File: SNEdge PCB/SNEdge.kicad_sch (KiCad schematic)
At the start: 40 parts, among them J1 RGB_OUT, U1 THS7376

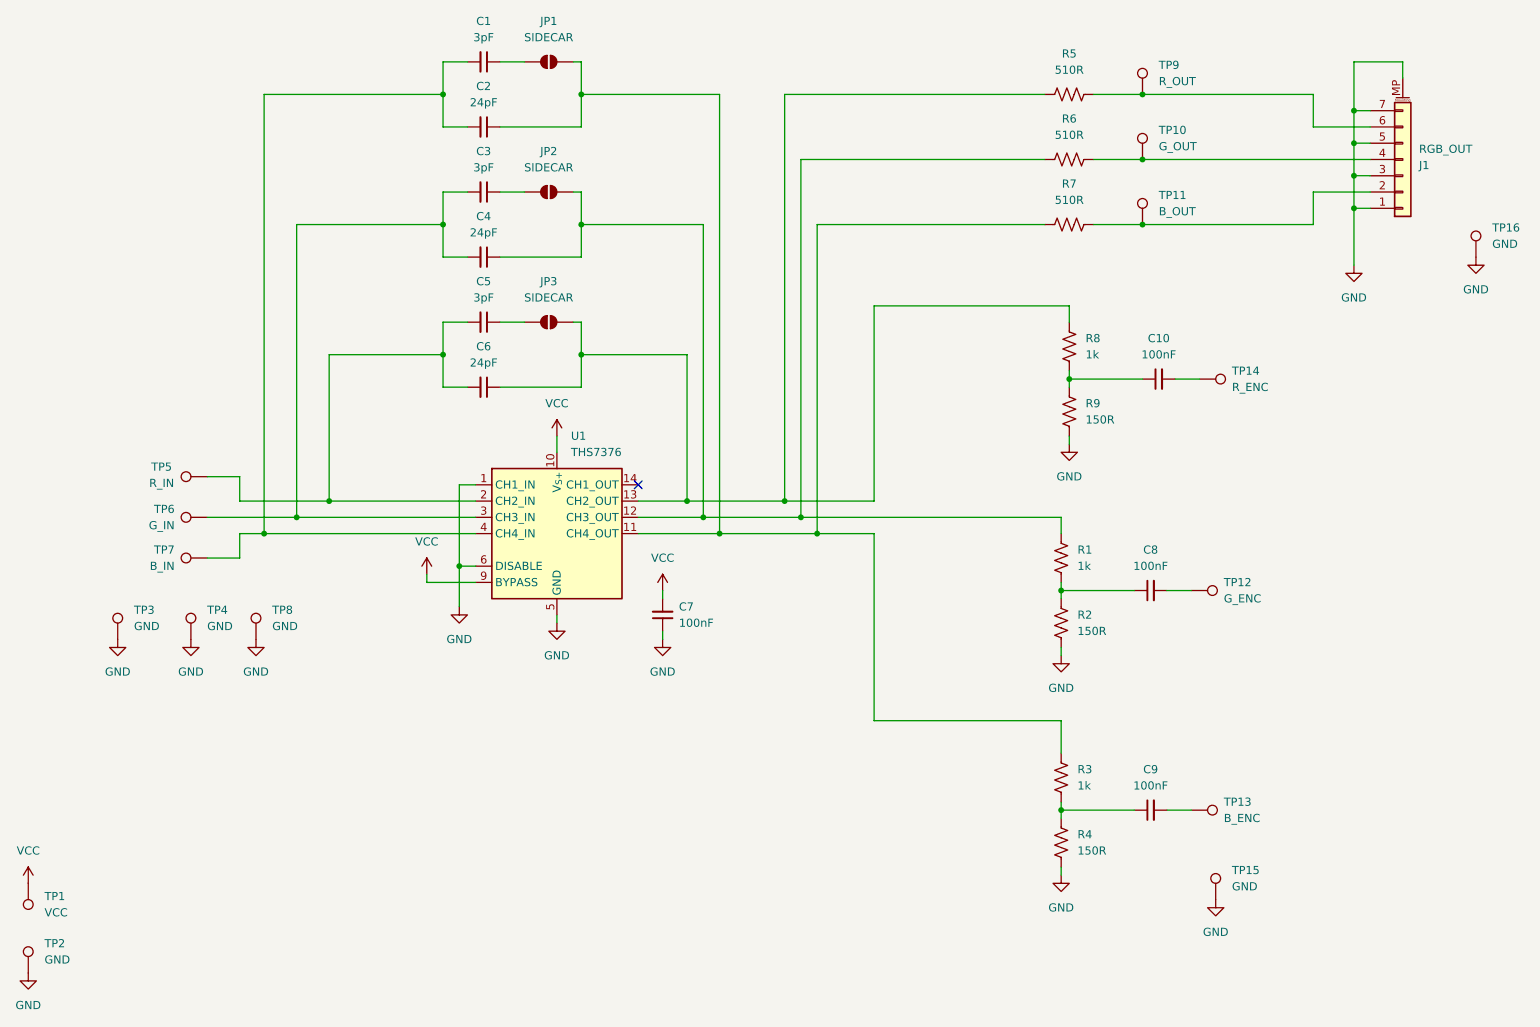
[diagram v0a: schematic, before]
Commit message: V2 based on RetroLoom's Rev2
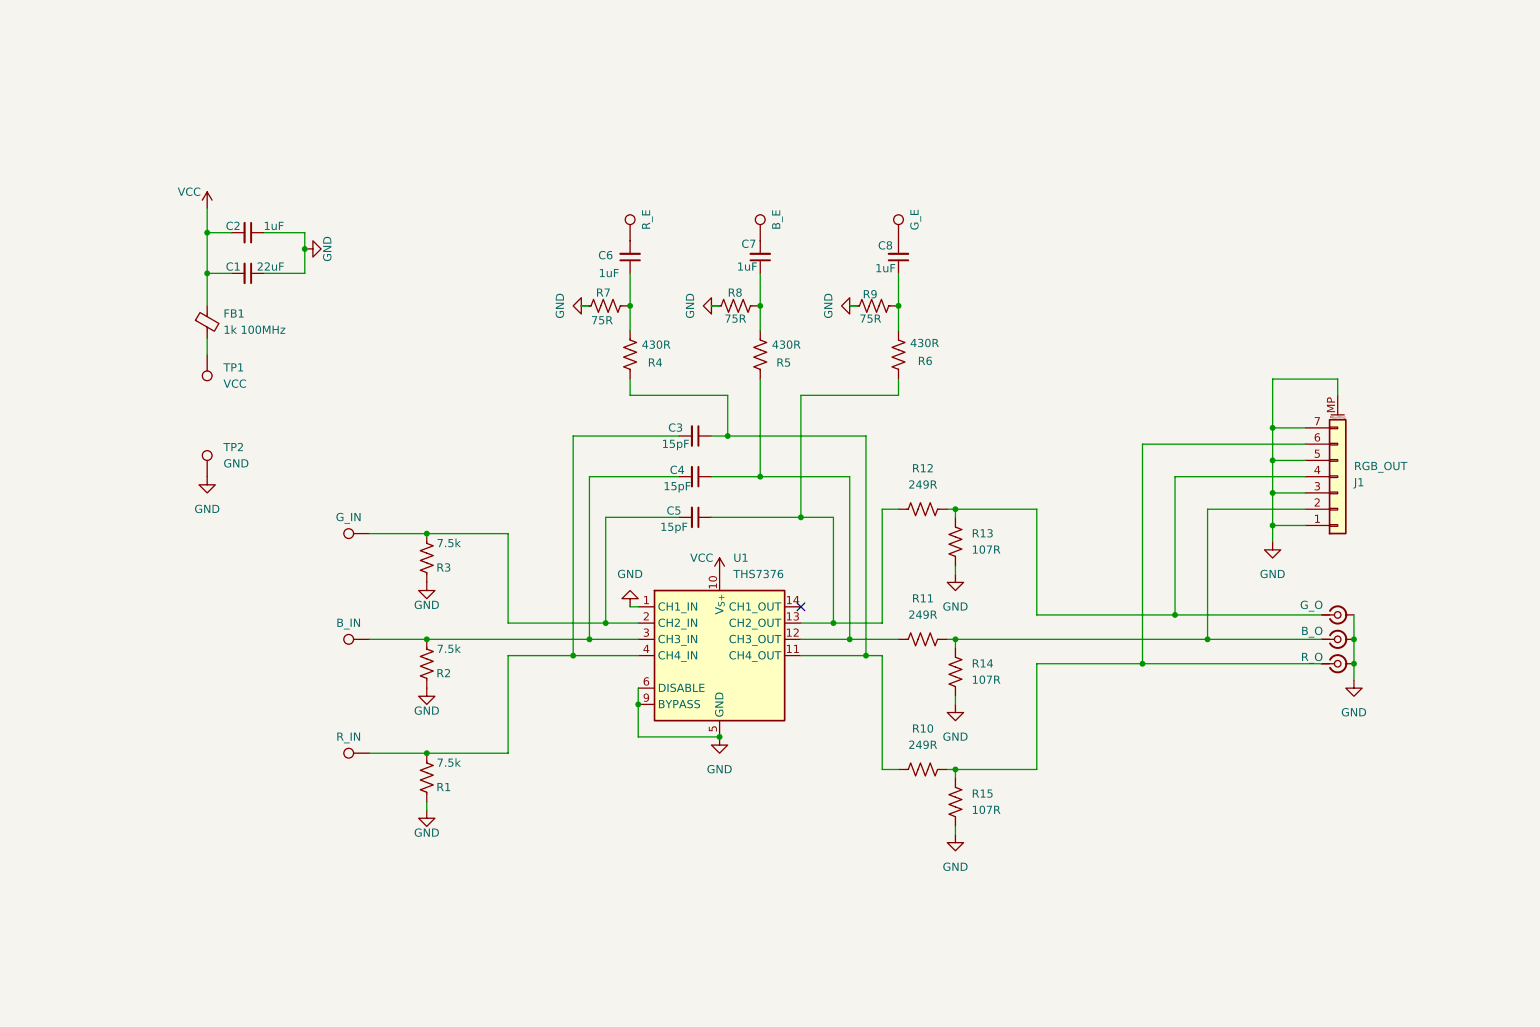
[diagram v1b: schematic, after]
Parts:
- removed C3, C5: 3pF, Capacitor_SMD:C_0805_2012Metric, symbol Device:C_Small
- removed C7: 100nF, Capacitor_SMD:C_0805_2012Metric, symbol Device:C_Small
- removed JP1, JP2, JP3: SIDECAR, Jumper:SolderJumper-2_P1.3mm_Open_RoundedPad1.0x1.5mm, symbol Jumper:SolderJumper_2_Open
- removed TP10: G_OUT, TestPoint:TestPoint_Pad_1.0x1.0mm, symbol Connector:TestPoint
- removed TP11: B_OUT, TestPoint:TestPoint_Pad_1.0x1.0mm, symbol Connector:TestPoint
- removed TP12: G_ENC, TestPoint:TestPoint_Pad_2.0x2.0mm, symbol Connector:TestPoint
- removed TP13: B_ENC, TestPoint:TestPoint_Pad_2.0x2.0mm, symbol Connector:TestPoint
- removed TP14: R_ENC, TestPoint:TestPoint_Pad_2.0x2.0mm, symbol Connector:TestPoint
- removed TP15: GND, TestPoint:TestPoint_Pad_2.0x2.0mm, symbol Connector:TestPoint
- removed TP16: GND, TestPoint:TestPoint_Pad_1.0x1.0mm, symbol Connector:TestPoint
- removed TP9: R_OUT, TestPoint:TestPoint_Pad_1.0x1.0mm, symbol Connector:TestPoint
- added C2: 1uF, Capacitor_SMD:C_0805_2012Metric_Pad1.18x1.45mm_HandSolder, symbol Device:C_Small
- added FB1: 1k 100MHz, Resistor_SMD:R_0805_2012Metric_Pad1.20x1.40mm_HandSolder, symbol Device:FerriteBead_Small
- added J10: R_O, Connector_Coaxial:U.FL_Hirose_U.FL-R-SMT-1_Vertical, symbol Connector:Conn_Coaxial_Small
- added J8: G_O, Connector_Coaxial:U.FL_Hirose_U.FL-R-SMT-1_Vertical, symbol Connector:Conn_Coaxial_Small
- added J9: B_O, Connector_Coaxial:U.FL_Hirose_U.FL-R-SMT-1_Vertical, symbol Connector:Conn_Coaxial_Small
- added R1, R2, R3: 7.5k, Resistor_SMD:R_0805_2012Metric_Pad1.20x1.40mm_HandSolder, symbol Device:R_US
- added R13, R14, R15: 107R, Resistor_SMD:R_0805_2012Metric_Pad1.20x1.40mm_HandSolder, symbol Device:R_US
- C1: value 3pF -> 22uF; footprint Capacitor_SMD:C_0805_2012Metric -> Capacitor_SMD:C_0805_2012Metric_Pad1.18x1.45mm_HandSolder; Digi_PN 311-1092-1-ND -> (none); MFG_PN CC0805CRNPO9BN3R0 -> (none)
- C3: renamed from C2; value 24pF -> 15pF; footprint Capacitor_SMD:C_0805_2012Metric -> Capacitor_SMD:C_0805_2012Metric_Pad1.18x1.45mm_HandSolder; Digi_PN 478-10387-1-ND -> (none); MFG_PN 08051A240FAT2A -> (none)
- C4: value 24pF -> 15pF; footprint Capacitor_SMD:C_0805_2012Metric -> Capacitor_SMD:C_0805_2012Metric_Pad1.18x1.45mm_HandSolder; Digi_PN 478-10387-1-ND -> (none); MFG_PN 08051A240FAT2A -> (none)
- C5: renamed from C6; value 24pF -> 15pF; footprint Capacitor_SMD:C_0805_2012Metric -> Capacitor_SMD:C_0805_2012Metric_Pad1.18x1.45mm_HandSolder; Digi_PN 478-10387-1-ND -> (none); MFG_PN 08051A240FAT2A -> (none)
- C6: renamed from C10; value 100nF -> 1uF; footprint Capacitor_SMD:C_0805_2012Metric -> Capacitor_SMD:C_0805_2012Metric_Pad1.18x1.45mm_HandSolder; Digi_PN 1276-2444-1-ND -> (none); MFG_PN CL21B104KBCNFNC -> (none)
- C7: renamed from C9; value 100nF -> 1uF; footprint Capacitor_SMD:C_0805_2012Metric -> Capacitor_SMD:C_0805_2012Metric_Pad1.18x1.45mm_HandSolder; Digi_PN 1276-2444-1-ND -> (none); MFG_PN CL21B104KBCNFNC -> (none)
- C8: value 100nF -> 1uF; footprint Capacitor_SMD:C_0805_2012Metric -> Capacitor_SMD:C_0805_2012Metric_Pad1.18x1.45mm_HandSolder; Digi_PN 1276-2444-1-ND -> (none); MFG_PN CL21B104KBCNFNC -> (none)
- R10: renamed from R7; value 510R -> 249R; footprint Resistor_SMD:R_0805_2012Metric -> Resistor_SMD:R_0805_2012Metric_Pad1.20x1.40mm_HandSolder; Digi_PN RMCF0805FT510RCT-ND -> (none); MFG_PN RMCF0805FT510R -> (none)
- R11: renamed from R6; value 510R -> 249R; footprint Resistor_SMD:R_0805_2012Metric -> Resistor_SMD:R_0805_2012Metric_Pad1.20x1.40mm_HandSolder; Digi_PN RMCF0805FT510RCT-ND -> (none); MFG_PN RMCF0805FT510R -> (none)
- R12: renamed from R5; value 510R -> 249R; footprint Resistor_SMD:R_0805_2012Metric -> Resistor_SMD:R_0805_2012Metric_Pad1.20x1.40mm_HandSolder; Digi_PN RMCF0805FT510RCT-ND -> (none); MFG_PN RMCF0805FT510R -> (none)
- R4: renamed from R8; value 1k -> 430R; footprint Resistor_SMD:R_0805_2012Metric -> Resistor_SMD:R_0805_2012Metric_Pad1.20x1.40mm_HandSolder; Digi_PN RMCF0805FT1K00CT-ND -> (none); MFG_PN RMCF0805FT1K00 -> (none)
- R5: renamed from R3; value 1k -> 430R; footprint Resistor_SMD:R_0805_2012Metric -> Resistor_SMD:R_0805_2012Metric_Pad1.20x1.40mm_HandSolder; Digi_PN RMCF0805FT1K00CT-ND -> (none); MFG_PN RMCF0805FT1K00 -> (none)
- R6: renamed from R1; value 1k -> 430R; footprint Resistor_SMD:R_0805_2012Metric -> Resistor_SMD:R_0805_2012Metric_Pad1.20x1.40mm_HandSolder; Digi_PN RMCF0805FT1K00CT-ND -> (none); MFG_PN RMCF0805FT1K00 -> (none)
- R7: renamed from R9; value 150R -> 75R; footprint Resistor_SMD:R_0805_2012Metric -> Resistor_SMD:R_0805_2012Metric_Pad1.20x1.40mm_HandSolder; Digi_PN RMCF0805FT150RCT-ND -> (none); MFG_PN RMCF0805FT150R -> (none)
- R8: renamed from R4; value 150R -> 75R; footprint Resistor_SMD:R_0805_2012Metric -> Resistor_SMD:R_0805_2012Metric_Pad1.20x1.40mm_HandSolder; Digi_PN RMCF0805FT150RCT-ND -> (none); MFG_PN RMCF0805FT150R -> (none)
- R9: renamed from R2; value 150R -> 75R; footprint Resistor_SMD:R_0805_2012Metric -> Resistor_SMD:R_0805_2012Metric_Pad1.20x1.40mm_HandSolder; Digi_PN RMCF0805FT150RCT-ND -> (none); MFG_PN RMCF0805FT150R -> (none)
- TP1, TP2, TP5: footprint TestPoint:TestPoint_Pad_2.0x2.0mm -> TestPoint:TestPoint_Pad_1.5x1.5mm
- TP3: value GND -> G_IN; footprint TestPoint:TestPoint_Pad_2.0x2.0mm -> TestPoint:TestPoint_Pad_1.5x1.5mm
- TP4: value GND -> B_IN; footprint TestPoint:TestPoint_Pad_2.0x2.0mm -> TestPoint:TestPoint_Pad_1.5x1.5mm
- TP6: value G_IN -> R_E; footprint TestPoint:TestPoint_Pad_2.0x2.0mm -> TestPoint:TestPoint_Pad_1.5x1.5mm
- TP7: value B_IN -> B_E; footprint TestPoint:TestPoint_Pad_2.0x2.0mm -> TestPoint:TestPoint_Pad_1.5x1.5mm
- TP8: value GND -> G_E; footprint TestPoint:TestPoint_Pad_2.0x2.0mm -> TestPoint:TestPoint_Pad_1.5x1.5mm
- U1: Digi_PN 296-40584-1-ND -> (none); MFG_PN THS7376IPWR -> (none)
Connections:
- net GND: now also C1.1, U1.9 (BYPASS), C2.1, J10.2 (Ext), J8.2 (Ext), J9.2 (Ext), R1.1, R13.2, R14.2, R15.2, R2.1, R3.1; no longer TP3.1, TP4.1, TP8.1
- net VCC: now also C1.2, C2.2, FB1.1; no longer TP1.1, U1.9 (BYPASS)
- net at C6.2: now also TP6.1
- net at C3.1, R10.2, U1.11 (CH4_OUT): now also R4.1; no longer R5.1
- net at C4.1, R11.2, U1.12 (CH3_OUT): now also R5.1; no longer R6.1
- net at C5.1, R12.2, U1.13 (CH2_OUT): now also R6.1; no longer R4.1
- net at C5.2, U1.2 (CH2_IN): now also TP3.1, R3.2; no longer TP5.1
- net at C4.2, U1.3 (CH3_IN): now also TP4.1, R2.2; no longer TP6.1
- net at C3.2, U1.4 (CH4_IN): now also TP5.1, R1.2; no longer C1.2, TP7.1
- net at R10.1: now also J1.6 (Pin_6), J10.1 (In), R15.1; no longer J1.2 (Pin_2)
- net at J1.4 (Pin_4): now also R12.1, J8.1 (In), R13.1; no longer R11.1
- net at C7.2: now also TP7.1
- net at C8.2: now also TP8.1
- new net: J1.2 (Pin_2), J9.1 (In), R11.1, R14.1
- new net: FB1.2, TP1.1
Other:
- company: Thunder Technologies -> Innov8bit
- moved on the sheet: C3, C4, C5, C6, C7, C8, J1, R10, R11, R12, R4, R5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

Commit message: Adjust feedback capacitors to 10pF
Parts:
- C3, C4, C5: value 15pF -> 10pF
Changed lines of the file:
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@@
 			)
 		)
-		(property "Value" "15pF"
+		(property "Value" "10pF"
 			(at 130.048 96.774 90)
 			(effects
@@
 			)
 		)
-		(property "Value" "15pF"
+		(property "Value" "10pF"
 			(at 130.302 83.82 90)
 			(effects
@@
 			)
 		)
-		(property "Value" "15pF"
+		(property "Value" "10pF"
 			(at 130.556 90.424 90)
 			(effects
